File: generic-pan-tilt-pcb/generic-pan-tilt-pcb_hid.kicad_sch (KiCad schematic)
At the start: 9 parts, among them SW3 219-12LPST, U5 MCP23017_SO

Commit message: fix c footprint for r
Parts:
- R15, R16, R17, R18, R19: footprint Capacitor_SMD:C_0402_1005Metric -> Resistor_SMD:R_0402_1005Metric
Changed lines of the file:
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@@
 			)
 		)
-		(property "Footprint" "Capacitor_SMD:C_0402_1005Metric"
+		(property "Footprint" "Resistor_SMD:R_0402_1005Metric"
 			(at 73.406 71.374 90)
 			(effects
@@
 			)
 		)
-		(property "Footprint" "Capacitor_SMD:C_0402_1005Metric"
+		(property "Footprint" "Resistor_SMD:R_0402_1005Metric"
 			(at 53.086 71.374 90)
 			(effects
@@
 			)
 		)
-		(property "Footprint" "Capacitor_SMD:C_0402_1005Metric"
+		(property "Footprint" "Resistor_SMD:R_0402_1005Metric"
 			(at 221.996 55.626 90)
 			(effects
@@
 			)
 		)
-		(property "Footprint" "Capacitor_SMD:C_0402_1005Metric"
+		(property "Footprint" "Resistor_SMD:R_0402_1005Metric"
 			(at 63.246 71.374 90)
 			(effects
@@
 			)
 		)
-		(property "Footprint" "Capacitor_SMD:C_0402_1005Metric"
+		(property "Footprint" "Resistor_SMD:R_0402_1005Metric"
 			(at 222.504 58.674 90)
 			(effects

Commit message: fix part numbers, add newark parts, separate fields for part desc
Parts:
- SW3: newark# (none) -> 74M3009
- U5: newark# (none) -> 41AH8461
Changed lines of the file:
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@@
+			)
+		)
+		(property "newark#" "74M3009"
+			(at 204.47 105.41 0)
+			(effects
+				(font
+					(size 1.27 1.27)
+				)
+				(hide yes)
 			)
 		)
@@
 			(at 110.49 81.28 0)
 			(effects
+				(font
+					(size 1.27 1.27)
+				)
+				(hide yes)
+			)
+		)
+		(property "newark#" "41AH8461"
+			(at 110.49 81.28 0)
+			(effects

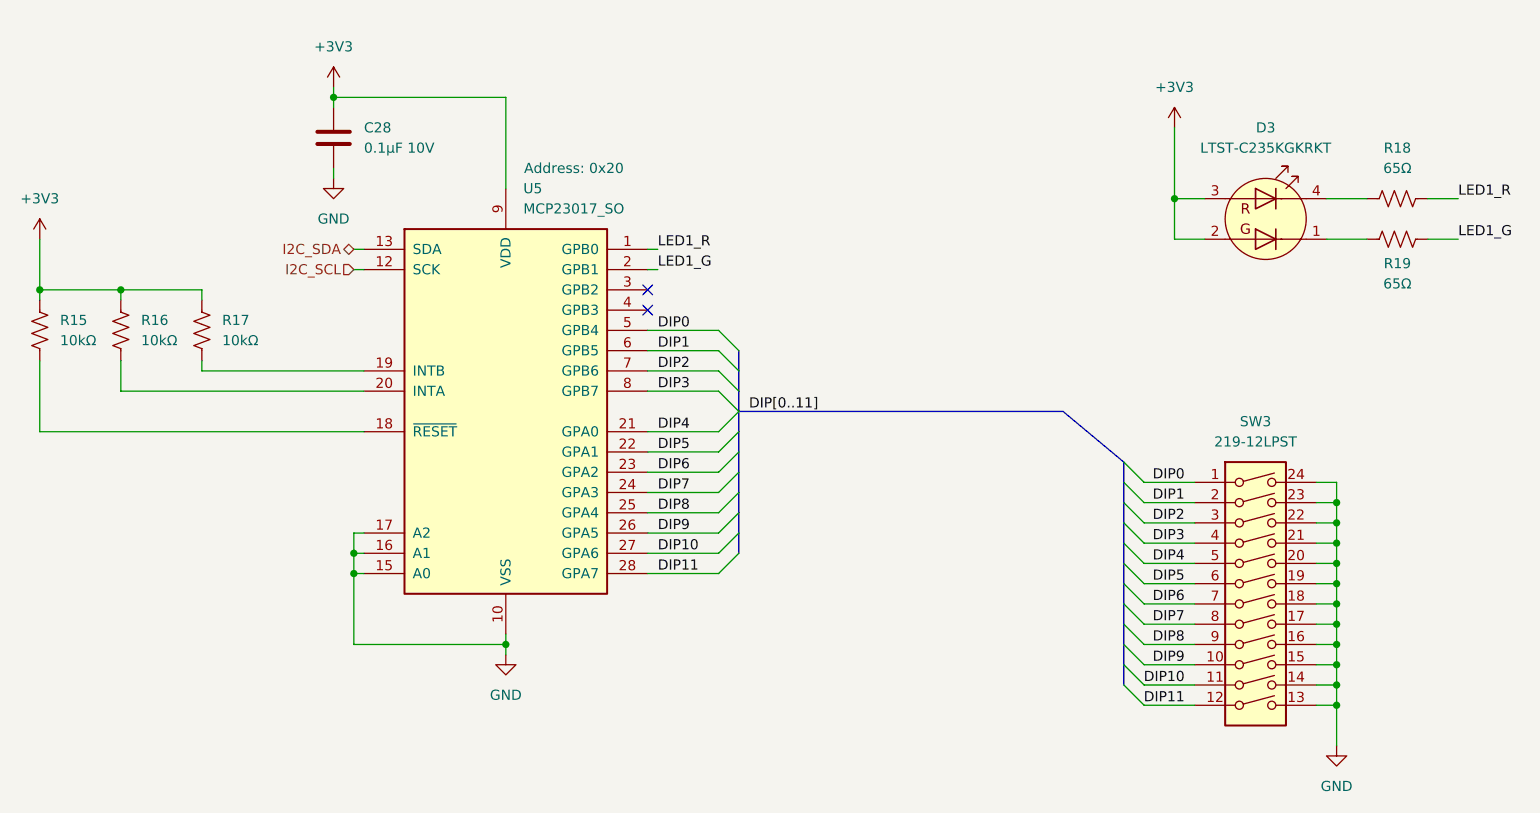
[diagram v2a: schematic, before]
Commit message: main board fix usb, fix uart, all caps and resistors manf and vendor, sch only replace psu and accel caps
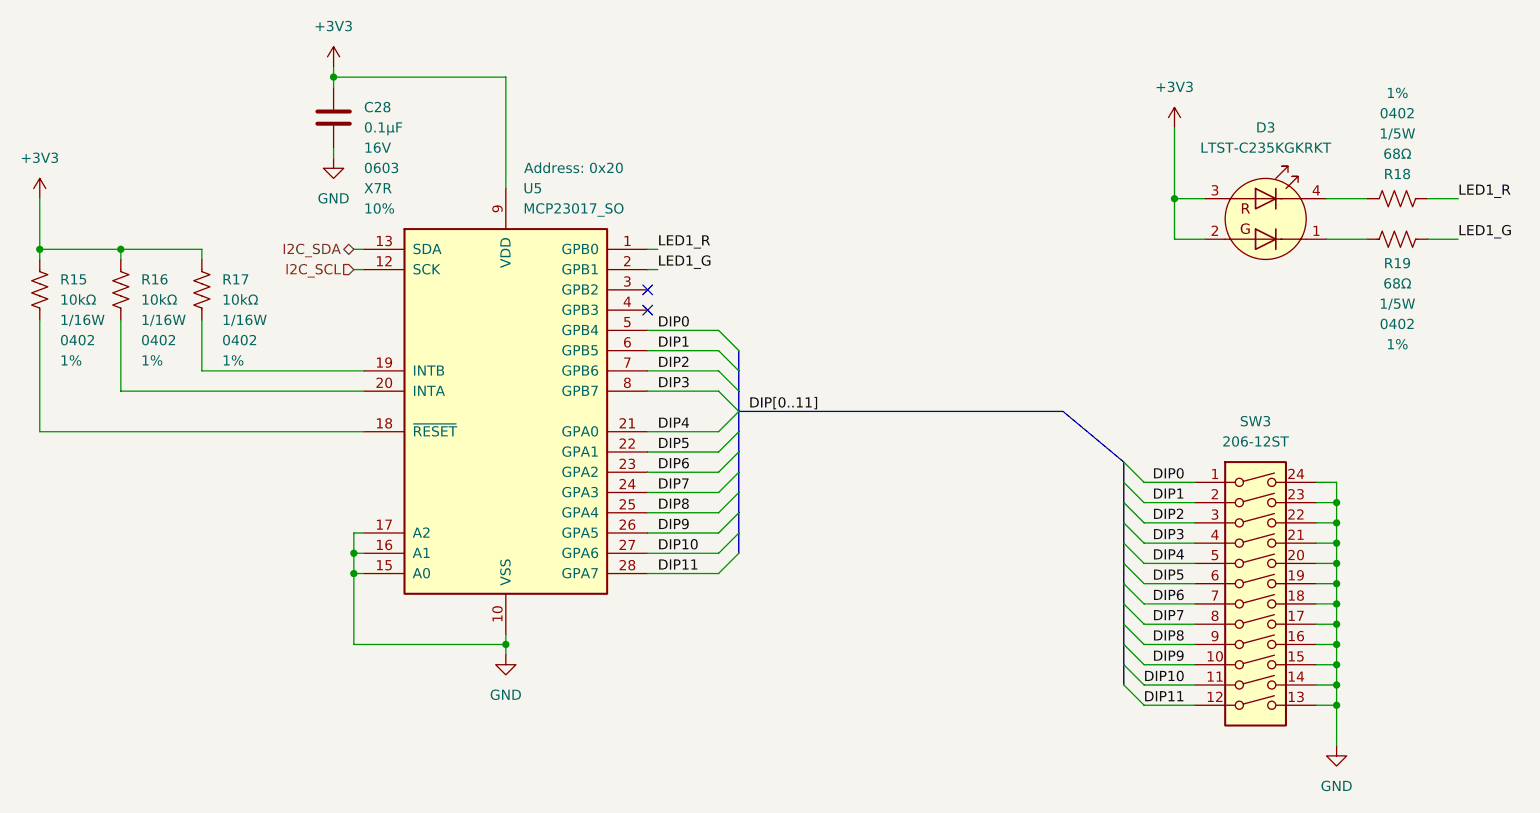
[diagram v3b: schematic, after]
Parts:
- C28: value 0.1µF 10V -> 0.1µF; footprint Capacitor_SMD:C_0402_1005Metric -> Capacitor_SMD:C_0603_1608Metric; Case Code (none) -> 0603; Dielectric (none) -> X7R; Tolerance (none) -> 10%; Voltage (none) -> 16V; digikey# (none) -> 1276-1005-1-ND; lcsc# (none) -> C66501; manf# (none) -> CL10B104KO8NNNC; mouser# (none) -> 187-CL10B104KO8NNNC; newark# (none) -> 82AC9325
- D3: lcsc# (none) -> C125110
- R15, R16, R17: Case Code (none) -> 0402; Power (none) -> 1/16W; Tolerance (none) -> 1%; digikey# (none) -> CR0402-FX-1002GLFCT-ND; lcsc# (none) -> C202396; manf# (none) -> CR0402-FX-1002GLF; mouser# (none) -> 652-CR0402FX-1002GLF; newark# (none) -> 06X5113
- R18, R19: value 65Ω -> 68Ω; Case Code (none) -> 0402; Power (none) -> 1/5W; Tolerance (none) -> 1%; digikey# (none) -> 541-10421-1-ND; lcsc# (none) -> C4068954; manf# (none) -> RCS040268R0FKED; mouser# (none) -> 71-RCS040268R0FKED
- SW3: value 219-12LPST -> 206-12ST; digikey# CT21912LPST-ND -> CT20612ST-ND; lcsc# (none) -> C2974278; manf# 219-12LPST -> 206-12ST; mouser# 774-21912LPST -> 774-20612ST; newark# 74M3009 -> 46F8099
- U5: lcsc# (none) -> C629440

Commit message: main fix mouser part extra space
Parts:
- R18, R19: mouser# 71-RCS040268R0FKED -> 71-RCS040268R0FKED
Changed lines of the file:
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@@
 			)
 		)
-		(property "mouser#" "71-RCS040268R0FKED "
+		(property "mouser#" "71-RCS040268R0FKED"
 			(at 222.25 54.61 0)
 			(effects
@@
 			)
 		)
-		(property "mouser#" "71-RCS040268R0FKED "
+		(property "mouser#" "71-RCS040268R0FKED"
 			(at 222.25 59.69 0)
 			(effects
